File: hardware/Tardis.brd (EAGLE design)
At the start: 100 x 80 mm, 51 parts, among them IC1 78LS05, IC2 ATMEGA328P-PU, IC3 ISD25120, J1 AUDIO IN, Q1 2N2222, Q2 N-CHAN, X1 LAMP, X2 POWER, X3 AMP PWR, X5 SPKR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

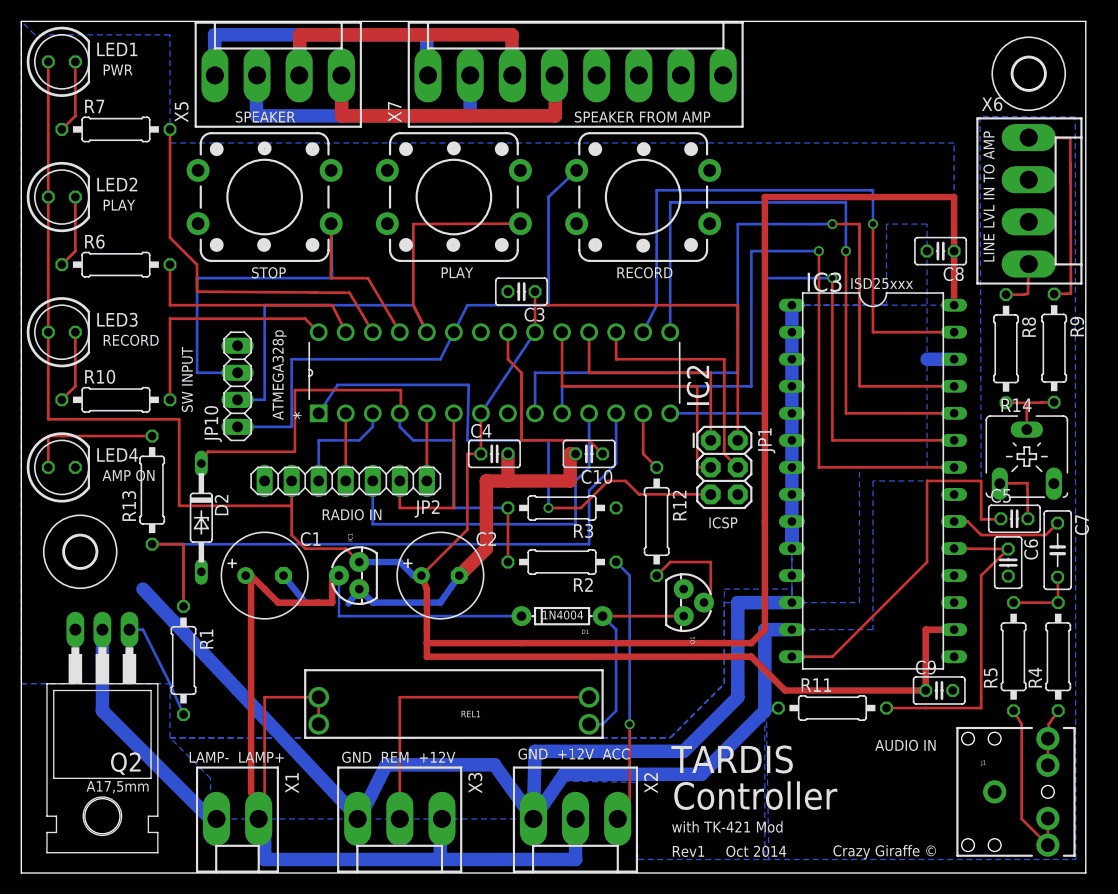
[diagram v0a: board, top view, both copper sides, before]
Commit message: Add custom library.
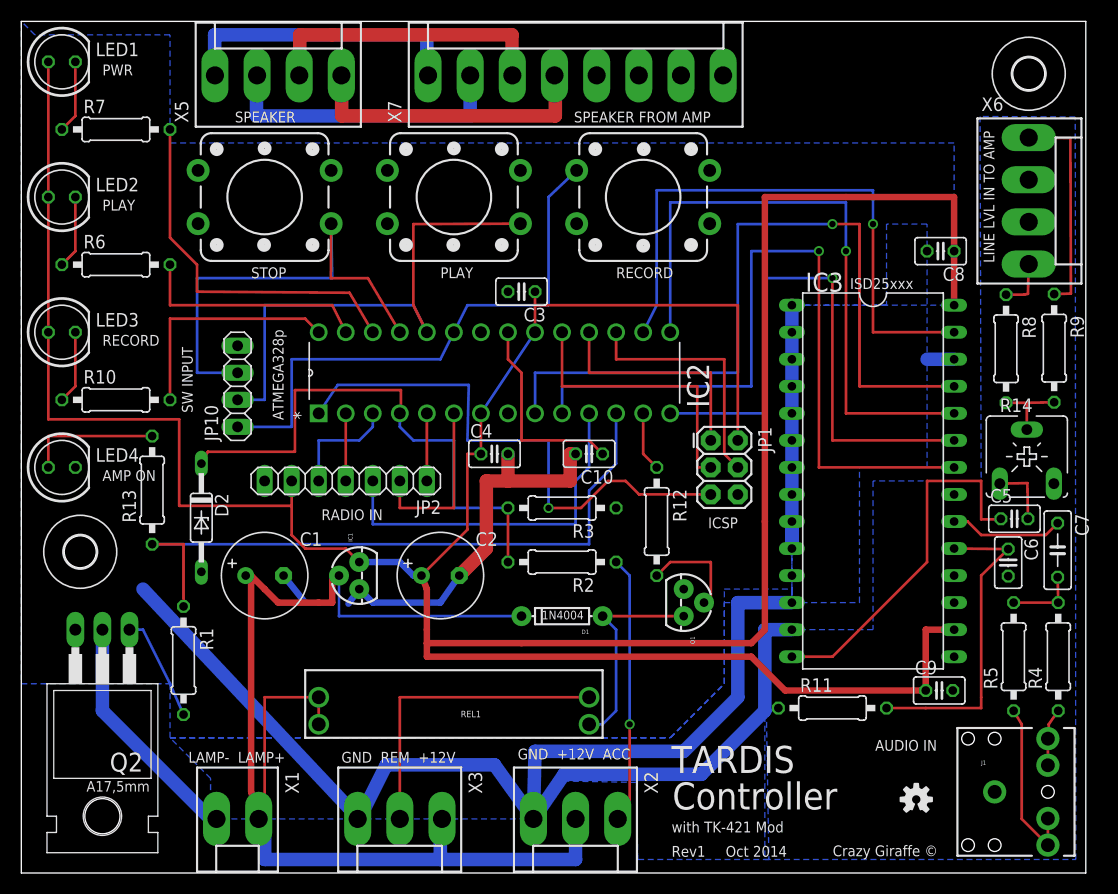
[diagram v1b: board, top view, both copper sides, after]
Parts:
- added U$3: (no value), SparkFun-Aesthetics:OSHW-LOGO-S
- IC2: device Atmel_By_element14_Batch_1:DIP254P762X457-28 -> CrazyGiraffe-Tardis:DIP254P762X457-28
- IC3: device crazygiraffe:DIL28-6 -> CrazyGiraffe-Tardis:CRAZYGIRAFFE_DIL28-6
- REL1: device crazygiraffe:RELAY-DIP -> CrazyGiraffe-Tardis:CRAZYGIRAFFE_RELAY-DIP
- S1, S2, S3: device crazygiraffe:TACTILE-PTH-12MM -> CrazyGiraffe-Tardis:CRAZYGIRAFFE_TACTILE-PTH-12MM
